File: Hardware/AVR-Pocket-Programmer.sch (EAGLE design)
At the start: 38 parts, among them Q1 12 MHz, U1 ATTINY2313-20S, U2 74ACT125D, X2 USBSMD

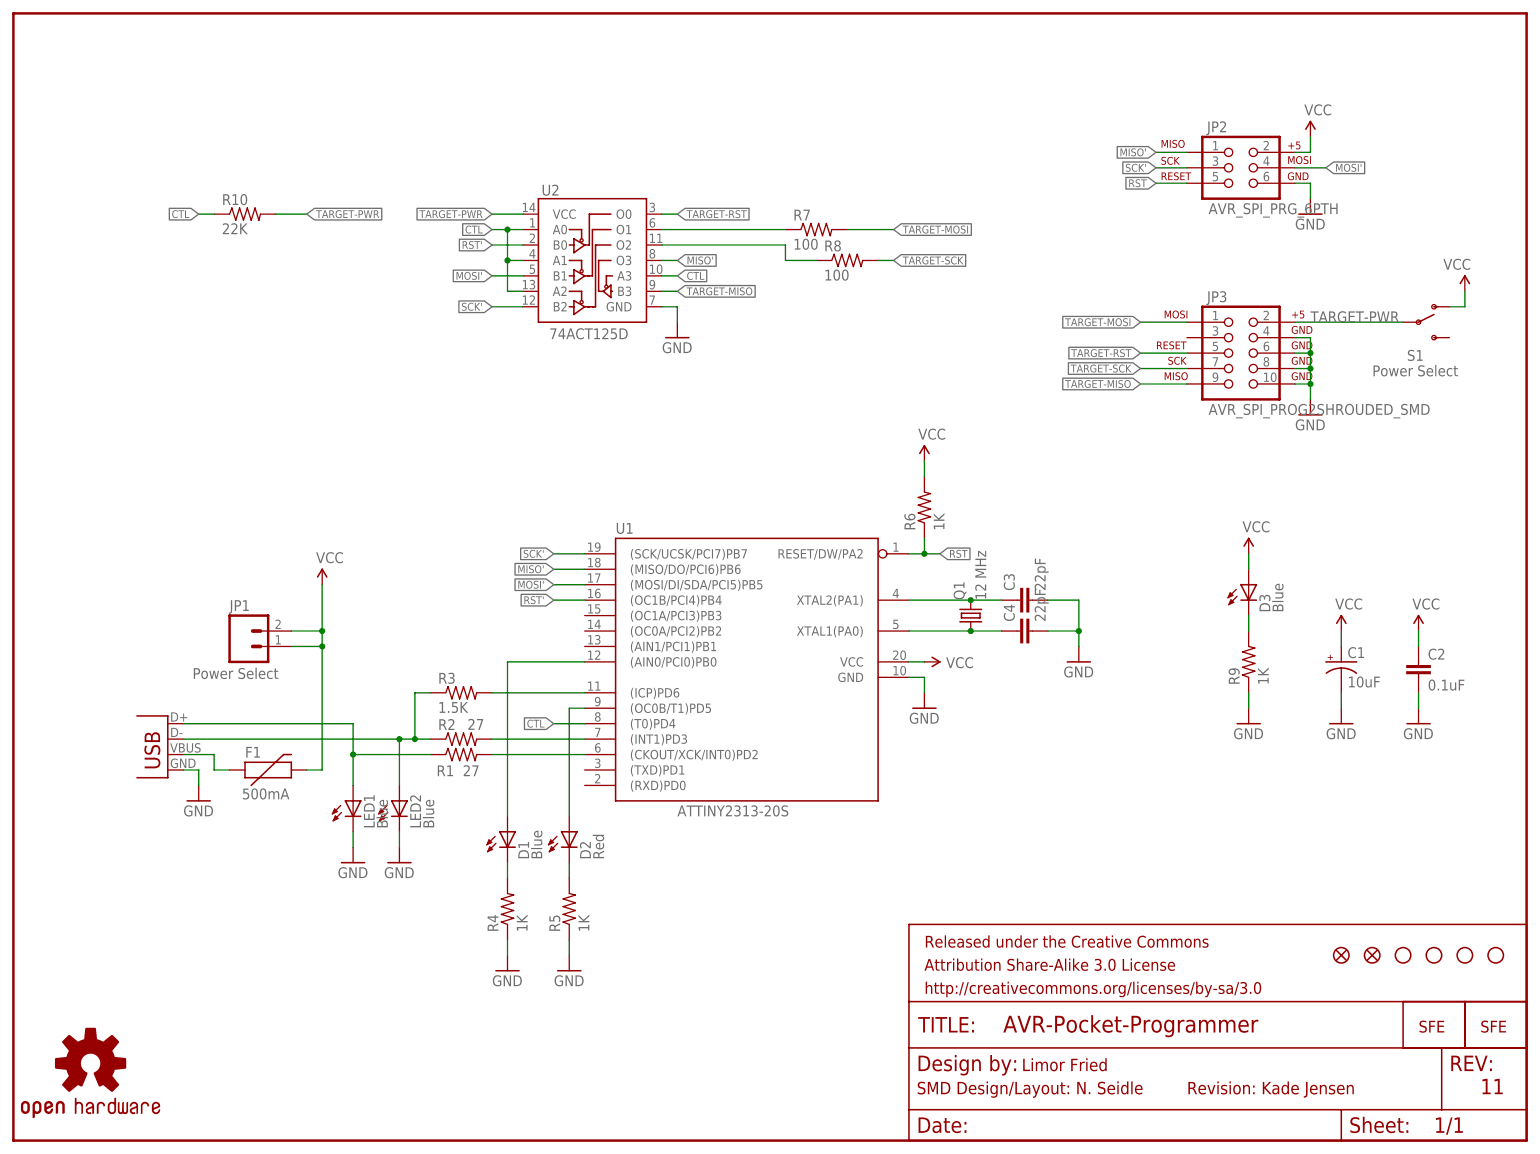
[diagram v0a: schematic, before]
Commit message: Removed branding and updated docs
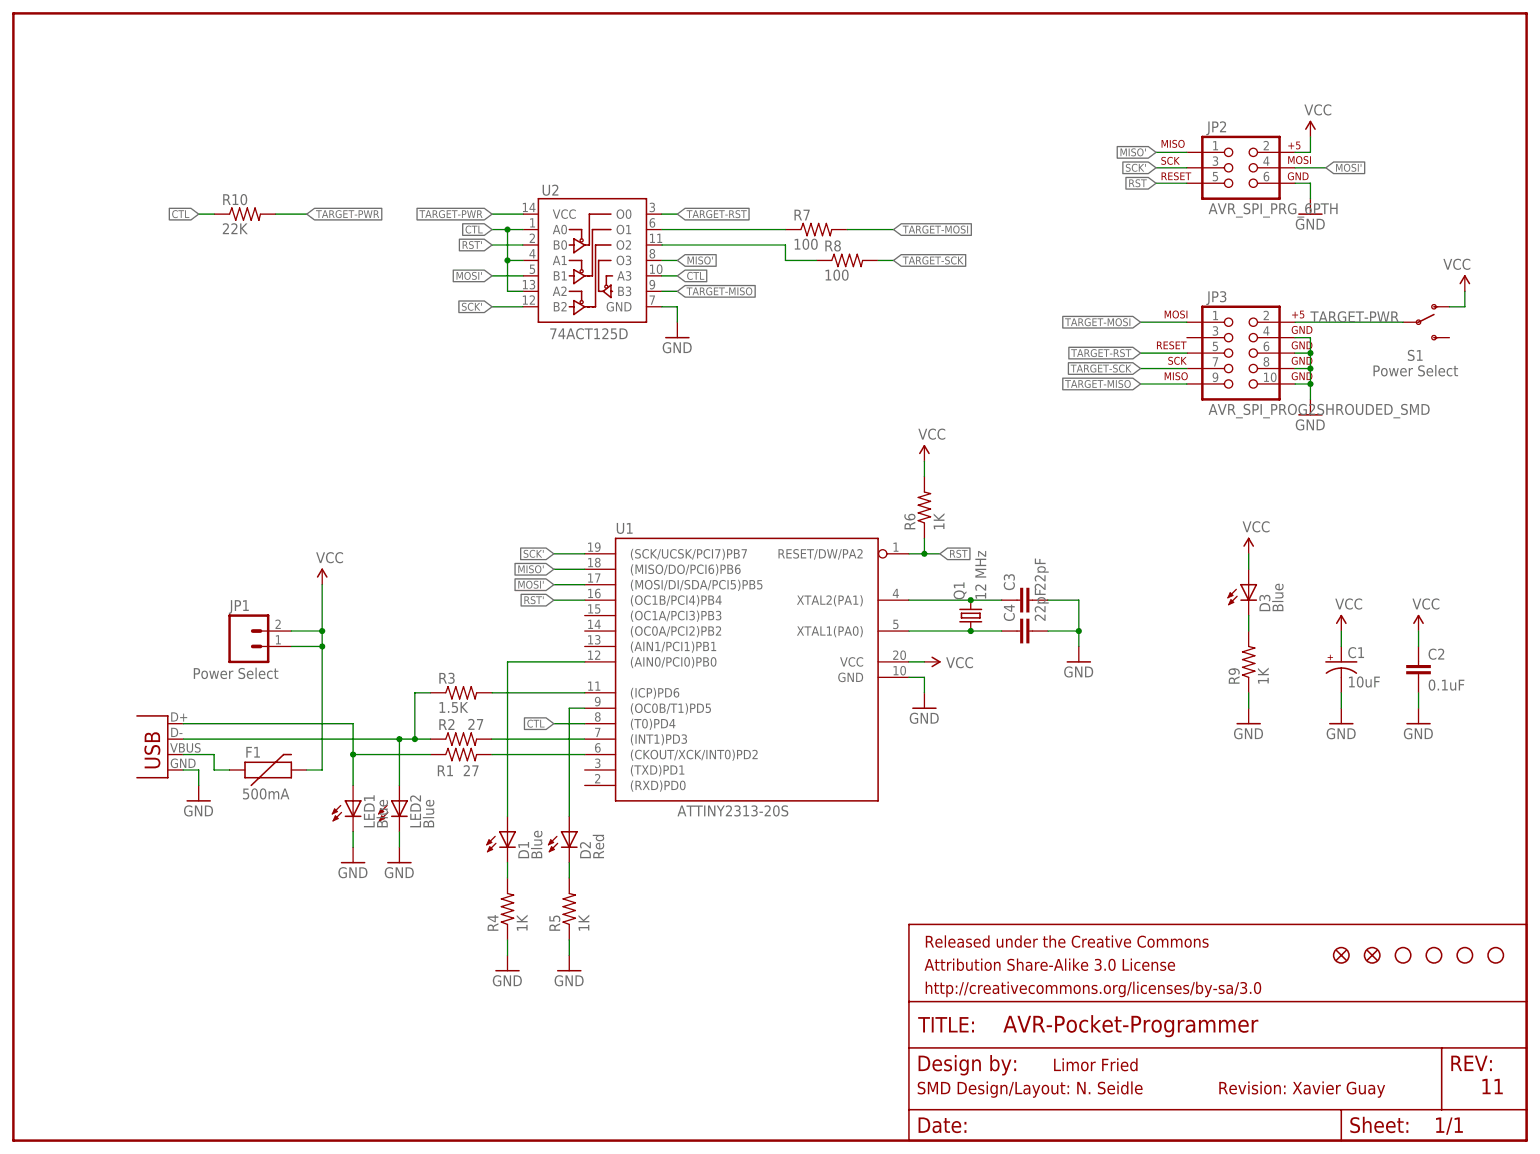
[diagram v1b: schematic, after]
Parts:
- removed LOGO1: OSHW-LOGOM, SparkFun-Aesthetics:OSHW-LOGOM
- removed U$2: LOGO-SFESK, SparkFun:LOGO-SFESK
- removed U$8: LOGO-SFENEW, SparkFun:LOGO-SFENEW
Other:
- note added: "Revision: Xavier Guay"
- note removed: "Revision: Kade Jensen"

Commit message: Board Updated
- Resized and rounded edges
- Changed to USB Micro B
- Moved some wires to fit Error Check
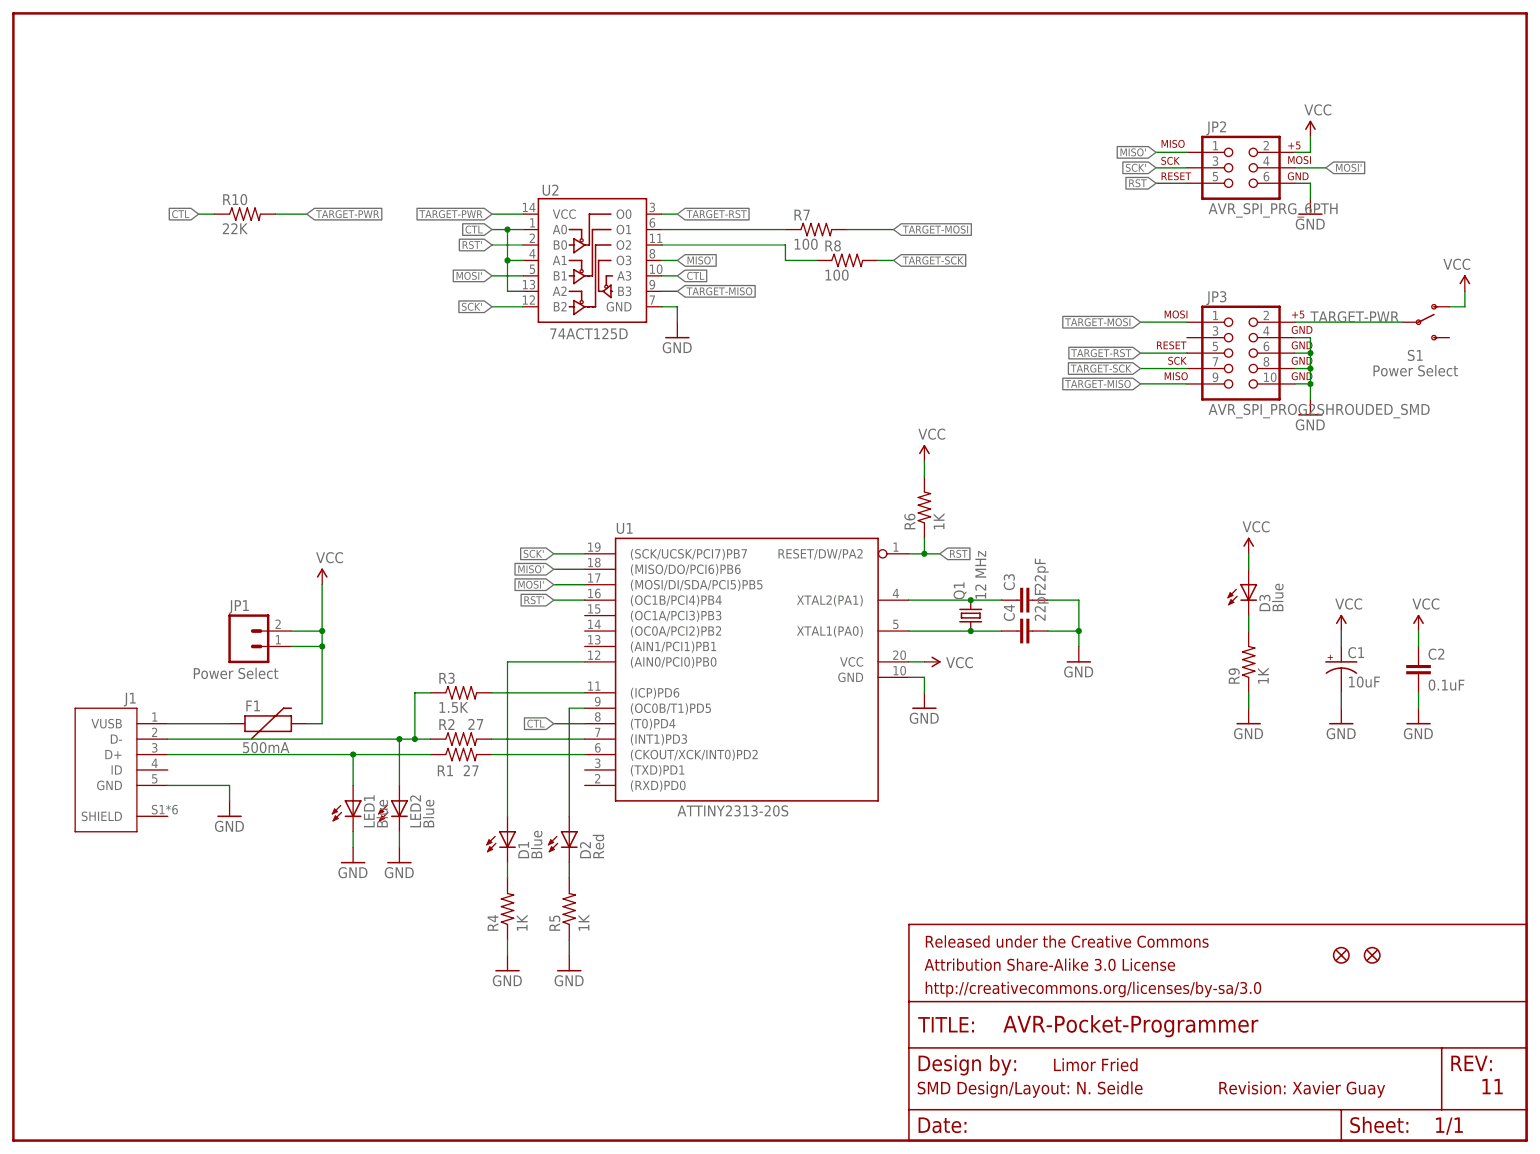
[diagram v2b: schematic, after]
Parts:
- removed U$1, U$3, U$4, U$5: STAND-OFF, SparkFun:STAND-OFF
- removed X2: USBSMD, SparkFun:USBSMD
- added J1: 10118193-0001LF, USB-Micro:10118193-0001LF
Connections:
- net D+: now also J1.D+; no longer X2.D+
- net D-: now also J1.D-; no longer X2.D-
- net GND: now also J1.GND; no longer X2.GND
- net N$4: now also J1.VUSB; no longer X2.VBUS
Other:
- moved on the sheet: F1
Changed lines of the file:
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@@
 <layer number="54" name="bGND_GNDA" color="1" fill="9" visible="no" active="no"/>
 <layer number="56" name="wert" color="7" fill="1" visible="no" active="no"/>
+<layer number="90" name="Modules" color="5" fill="1" visible="yes" active="yes"/>
 <layer number="91" name="Nets" color="2" fill="1" visible="yes" active="yes"/>
 <layer number="92" name="Busses" color="1" fill="1" visible="yes" active="yes"/>
@@
 </classes>
 <parts>
-<part name="X2" library="SparkFun" deviceset="USB" device="SMD"/>
 <part name="U1" library="avr" deviceset="ATTINY2313" device="S" technology="-20"/>
 <part name="C2" library="SparkFun" deviceset="CAP" device="0603-CAP" value="0.1uF"/>
@@
 <part name="P+11" library="SparkFun" deviceset="VCC" device=""/>
 <part name="GND16" library="SparkFun" deviceset="GND" device=""/>
-<part name="U$1" library="SparkFun" deviceset="STAND-OFF" device=""/>
-<part name="U$3" library="SparkFun" deviceset="STAND-OFF" device=""/>
-<part name="U$4" library="SparkFun" deviceset="STAND-OFF" device=""/>
-<part name="U$5" library="SparkFun" deviceset="STAND-OFF" device=""/>
 <part name="U$6" library="SparkFun" deviceset="FIDUCIAL" device="1X2"/>
 <part name="U$7" library="SparkFun" deviceset="FIDUCIAL" device="1X2"/>
@@
 <part name="R10" library="SparkFun" deviceset="RESISTOR" device="0603-RES" value="22K"/>
 <part name="FRAME1" library="SparkFun-Aesthetics" deviceset="FRAME-LETTER" device=""/>
+<part name="J1" library="USB-Micro" deviceset="10118193-0001LF" device=""/>
 </parts>
 <sheets>
@@
 </plain>
 <instances>
-<instance part="X2" gate="G$1" x="25.4" y="60.96" smashed="yes" rot="MR0"/>
 <instance part="U1" gate="G$1" x="121.92" y="76.2" smashed="yes" rot="MR0">
 <attribute name="NAME" x="99.06" y="99.822" size="1.778" layer="95"/>
@@
 <attribute name="VALUE" x="49.784" y="94.996" size="1.778" layer="96"/>
 </instance>
-<instance part="GND7" gate="1" x="30.48" y="55.88" smashed="yes">
-<attribute name="VALUE" x="27.94" y="53.34" size="1.778" layer="96"/>
+<instance part="GND7" gate="1" x="35.56" y="53.34" smashed="yes">
+<attribute name="VALUE" x="33.02" y="50.8" size="1.778" layer="96"/>
 </instance>
 <instance part="R1" gate="G$1" x="73.66" y="63.5" smashed="yes">
@@
 <attribute name="VALUE" x="147.32" y="68.58" size="1.778" layer="96"/>
 </instance>
-<instance part="U$1" gate="G$1" x="243.84" y="30.48" smashed="yes"/>
-<instance part="U$3" gate="G$1" x="238.76" y="30.48" smashed="yes"/>
-<instance part="U$4" gate="G$1" x="233.68" y="30.48" smashed="yes"/>
-<instance part="U$5" gate="G$1" x="228.6" y="30.48" smashed="yes"/>
 <instance part="U$6" gate="G$1" x="223.52" y="30.48" smashed="yes"/>
 <instance part="U$7" gate="G$1" x="218.44" y="30.48" smashed="yes"/>
@@
 <attribute name="VALUE" x="202.184" y="100.076" size="1.778" layer="96"/>
 </instance>
-<instance part="F1" gate="G$1" x="40.64" y="60.96" smashed="yes">
-<attribute name="NAME" x="38.1" y="62.992" size="1.778" layer="95"/>
-<attribute name="VALUE" x="37.592" y="56.134" size="1.778" layer="96"/>
+<instance part="F1" gate="G$1" x="40.64" y="68.58" smashed="yes">
+<attribute name="NAME" x="38.1" y="70.612" size="1.778" layer="95"/>
+<attribute name="VALUE" x="37.592" y="63.754" size="1.778" layer="96"/>
 </instance>
 <instance part="LED1" gate="G$1" x="55.88" y="55.88" smashed="yes">
@@
 <attribute name="DRAWING_NAME" x="162.814" y="17.78" size="2.7432" layer="94" font="vector"/>
 </instance>
+<instance part="J1" gate="G$1" x="15.24" y="60.96" smashed="yes" rot="MR0">
+<attribute name="NAME" x="20.32165" y="71.8886" size="1.778" layer="95" rot="MR0"/>
+</instance>
 </instances>
 <busses>
@@
 <net name="VCC" class="0">
 <segment>
-<wire x1="50.8" y1="60.96" x2="50.8" y2="81.28" width="0.1524" layer="91"/>
 <wire x1="50.8" y1="81.28" x2="50.8" y2="83.82" width="0.1524" layer="91"/>
 <wire x1="50.8" y1="83.82" x2="50.8" y2="91.44" width="0.1524" layer="91"/>
 <wire x1="45.72" y1="83.82" x2="50.8" y2="83.82" width="0.1524" layer="91"/>
 <wire x1="45.72" y1="81.28" x2="50.8" y2="81.28" width="0.1524" layer="91"/>
-<wire x1="48.26" y1="60.96" x2="50.8" y2="60.96" width="0.1524" layer="91"/>
 <junction x="50.8" y="83.82"/>
-<junction x="50.8" y="81.28"/>
 <pinref part="P+4" gate="1" pin="VCC"/>
 <pinref part="JP1" gate="G$1" pin="2"/>
 <pinref part="JP1" gate="G$1" pin="1"/>
 <pinref part="F1" gate="G$1" pin="2"/>
+<wire x1="50.8" y1="68.58" x2="50.8" y2="81.28" width="0.1524" layer="91"/>
+<junction x="50.8" y="81.28"/>
+<wire x1="48.26" y1="68.58" x2="50.8" y2="68.58" width="0.1524" layer="91"/>
 </segment>
 <segment>
@@
 </net>
 <net name="GND" class="0">
-<segment>
-<wire x1="27.94" y1="60.96" x2="30.48" y2="60.96" width="0.1524" layer="91"/>
-<wire x1="30.48" y1="60.96" x2="30.48" y2="58.42" width="0.1524" layer="91"/>
-<pinref part="X2" gate="G$1" pin="GND"/>
-<pinref part="GND7" gate="1" pin="GND"/>
-</segment>
 <segment>
 <wire x1="231.14" y1="71.12" x2="231.14" y2="73.66" width="0.1524" layer="91"/>
@@
 <pinref part="C4" gate="G$1" pin="2"/>
 </segment>
+<segment>
+<pinref part="J1" gate="G$1" pin="GND"/>
+<pinref part="GND7" gate="1" pin="GND"/>
+<wire x1="35.56" y1="55.88" x2="35.56" y2="58.42" width="0.1524" layer="91"/>
+<wire x1="35.56" y1="58.42" x2="25.4" y2="58.42" width="0.1524" layer="91"/>
+</segment>
 </net>
 <net name="RST" class="0">
@@
 <net name="D-" class="0">
 <segment>
-<wire x1="27.94" y1="66.04" x2="63.5" y2="66.04" width="0.1524" layer="91"/>
+<wire x1="25.4" y1="66.04" x2="63.5" y2="66.04" width="0.1524" layer="91"/>
 <wire x1="63.5" y1="66.04" x2="66.04" y2="66.04" width="0.1524" layer="91"/>
 <wire x1="66.04" y1="66.04" x2="68.58" y2="66.04" width="0.1524" layer="91"/>
@@
 <junction x="66.04" y="66.04"/>
 <junction x="63.5" y="66.04"/>
-<pinref part="X2" gate="G$1" pin="D-"/>
 <pinref part="R2" gate="G$1" pin="1"/>
 <pinref part="R3" gate="G$1" pin="1"/>
 <pinref part="LED2" gate="G$1" pin="A"/>
+<pinref part="J1" gate="G$1" pin="D-"/>
 </segment>
 </net>
 <net name="D+" class="0">
 <segment>
-<wire x1="27.94" y1="68.58" x2="55.88" y2="68.58" width="0.1524" layer="91"/>
-<wire x1="55.88" y1="68.58" x2="55.88" y2="63.5" width="0.1524" layer="91"/>
+<wire x1="25.4" y1="63.5" x2="55.88" y2="63.5" width="0.1524" layer="91"/>
 <wire x1="55.88" y1="63.5" x2="68.58" y2="63.5" width="0.1524" layer="91"/>
 <wire x1="55.88" y1="58.42" x2="55.88" y2="63.5" width="0.1524" layer="91"/>
 <junction x="55.88" y="63.5"/>
-<pinref part="X2" gate="G$1" pin="D+"/>
 <pinref part="R1" gate="G$1" pin="1"/>
 <pinref part="LED1" gate="G$1" pin="A"/>
+<pinref part="J1" gate="G$1" pin="D+"/>
 </segment>
 </net>
@@
 </segment>
 </net>
-<net name="N$4" class="0">
-<segment>
-<wire x1="35.56" y1="60.96" x2="33.02" y2="60.96" width="0.1524" layer="91"/>
-<wire x1="33.02" y1="60.96" x2="33.02" y2="63.5" width="0.1524" layer="91"/>
-<wire x1="33.02" y1="63.5" x2="27.94" y2="63.5" width="0.1524" layer="91"/>
-<pinref part="F1" gate="G$1" pin="1"/>
-<pinref part="X2" gate="G$1" pin="VBUS"/>
-</segment>
-</net>
 <net name="N$5" class="0">
 <segment>
@@
 </segment>
 </net>
+<net name="N$4" class="0">
+<segment>
+<pinref part="F1" gate="G$1" pin="1"/>
+<pinref part="J1" gate="G$1" pin="VUSB"/>
+<wire x1="35.56" y1="68.58" x2="25.4" y2="68.58" width="0.1524" layer="91"/>
+</segment>
+</net>
